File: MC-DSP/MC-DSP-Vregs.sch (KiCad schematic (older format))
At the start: 12 parts, among them IC1 R-78E5.0-0.5, T1 R-78E3.3-0.5

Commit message: updated top level of schematic with "to test" and "to do" notes
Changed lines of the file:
@@
 $Descr A4 11693 8268
 encoding utf-8
-Sheet 5 6
+Sheet 5 9
 Title ""
 Date ""
@@
 	6300 4225 6600 4225
 Connection ~ 6300 4225
-Text Notes 6850 3525 0    50   ~ 0
+Text Notes 2300 4000 0    50   ~ 0
 Toss this if dac buffs dont need it\n
 Text Notes 7175 5250 0    50   ~ 0

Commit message: ADC refs, FTDI changes, and more
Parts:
- removed C? (x2): 10 uF, Capacitor_SMD:C_0603_1608Metric, symbol Device:C_Small
- removed C? (x2): 4.7 uF, Capacitor_SMD:C_0603_1608Metric, symbol Device:C_Small
- removed C? (x2): 22 uF, Capacitor_SMD:C_0603_1608Metric, symbol Device:C_Small
- removed IC1: R-78E5.0-0.5, R78E5005, symbol R-78E5.0-0.5:R-78E5.0-0.5
- removed L? (x2): 12 uH, symbol Device:L_Small
- removed T1: R-78E3.3-0.5, R78E1205, symbol R-78E3.3-0.5:R-78E3.3-0.5
- added C? (x6): 2.2uF, symbol Device:C
- added C?: 10 uF, Capacitor_SMD:C_0603_1608Metric, symbol Device:C_Small
- added C?: 4.7 uF, Capacitor_SMD:C_0603_1608Metric, symbol Device:C_Small
- added C?: 22 uF, Capacitor_SMD:C_0603_1608Metric, symbol Device:C_Small
- added FB? (x3): Ferrite_Bead, symbol Device:Ferrite_Bead
- added L?: 12 uH, symbol Device:L_Small
- added T?: R-78E3.3-0.5, R78E1205, symbol R-78E3.3-0.5:R-78E3.3-0.5
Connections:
- net labels added: VDDA
- net labels removed: +5V
- wire segments 32 -> 40
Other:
- note added: "VDDA_3V3"
- note added: "VDD_1V2"
- note added: "VDD_3V3\n"
- note removed: "Toss this if dac buffs dont need it\n"
- moved on the sheet: C?

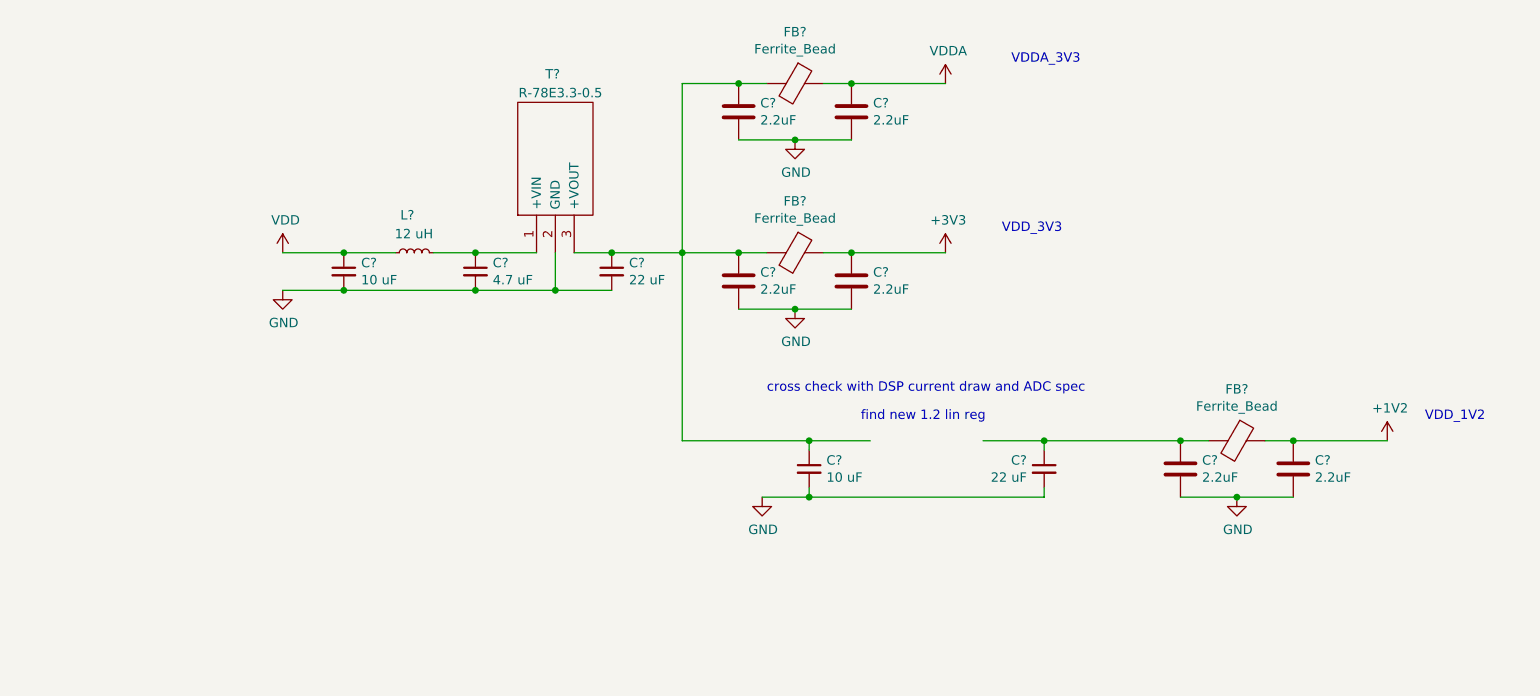
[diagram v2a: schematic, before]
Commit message: All parts labeled, just need to pick passives basically.
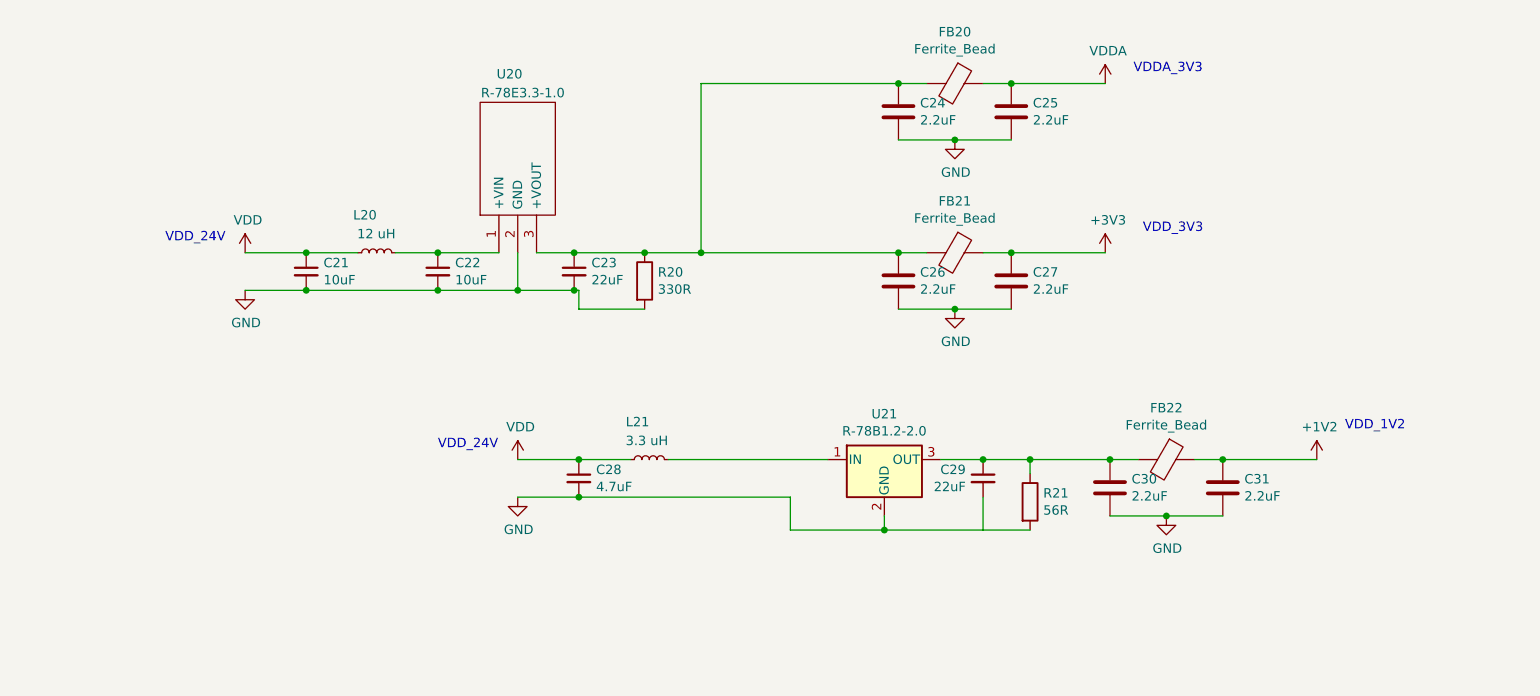
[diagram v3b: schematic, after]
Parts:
- removed C?: 10 uF, Capacitor_SMD:C_0603_1608Metric, symbol Device:C_Small
- added C28: 4.7uF, Capacitor_SMD:C_0201_0603Metric_Pad0.64x0.40mm_HandSolder, symbol Device:C_Small
- added L21: 3.3 uH, ?, symbol Device:L_Small
- added R20: 330R, Resistor_SMD:R_0603_1608Metric_Pad0.98x0.95mm_HandSolder, symbol Device:R
- added R21: 56R, Resistor_SMD:R_0603_1608Metric_Pad0.98x0.95mm_HandSolder, symbol Device:R
- added U21: R-78B1.2-2.0, Converter_DCDC:Converter_DCDC_RECOM_R-78B-2.0_THT, symbol Regulator_Switching:R-78B1.2-2.0
- C21: renamed from C?; value 10 uF -> 10uF; footprint Capacitor_SMD:C_0603_1608Metric -> Capacitor_SMD:C_0201_0603Metric_Pad0.64x0.40mm_HandSolder
- C22: renamed from C?; value 4.7 uF -> 10uF; footprint Capacitor_SMD:C_0603_1608Metric -> Capacitor_SMD:C_0201_0603Metric_Pad0.64x0.40mm_HandSolder
- C23, C29: renamed from C?; value 22 uF -> 22uF; footprint Capacitor_SMD:C_0603_1608Metric -> Capacitor_SMD:C_0201_0603Metric_Pad0.64x0.40mm_HandSolder
- C24, C25, C26, C27, C30, C31: renamed from C?; footprint (none) -> Capacitor_SMD:C_0201_0603Metric_Pad0.64x0.40mm_HandSolder
- FB20, FB21, FB22: renamed from FB?; footprint (none) -> ?
- L20: renamed from L?; footprint (none) -> ?
- U20: renamed from T?; value R-78E3.3-0.5 -> R-78E3.3-1.0
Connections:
- wire segments 40 -> 47
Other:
- note added: "VDD_24V"
- note removed: "cross check with DSP current draw and ADC spec"
- note removed: "find new 1.2 lin reg\n"
- moved on the sheet: C21, C22, C23, C24, C25, C26, C27, C29, C30, C31, FB20, FB21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

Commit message: DSP - added footprints and links to most parts
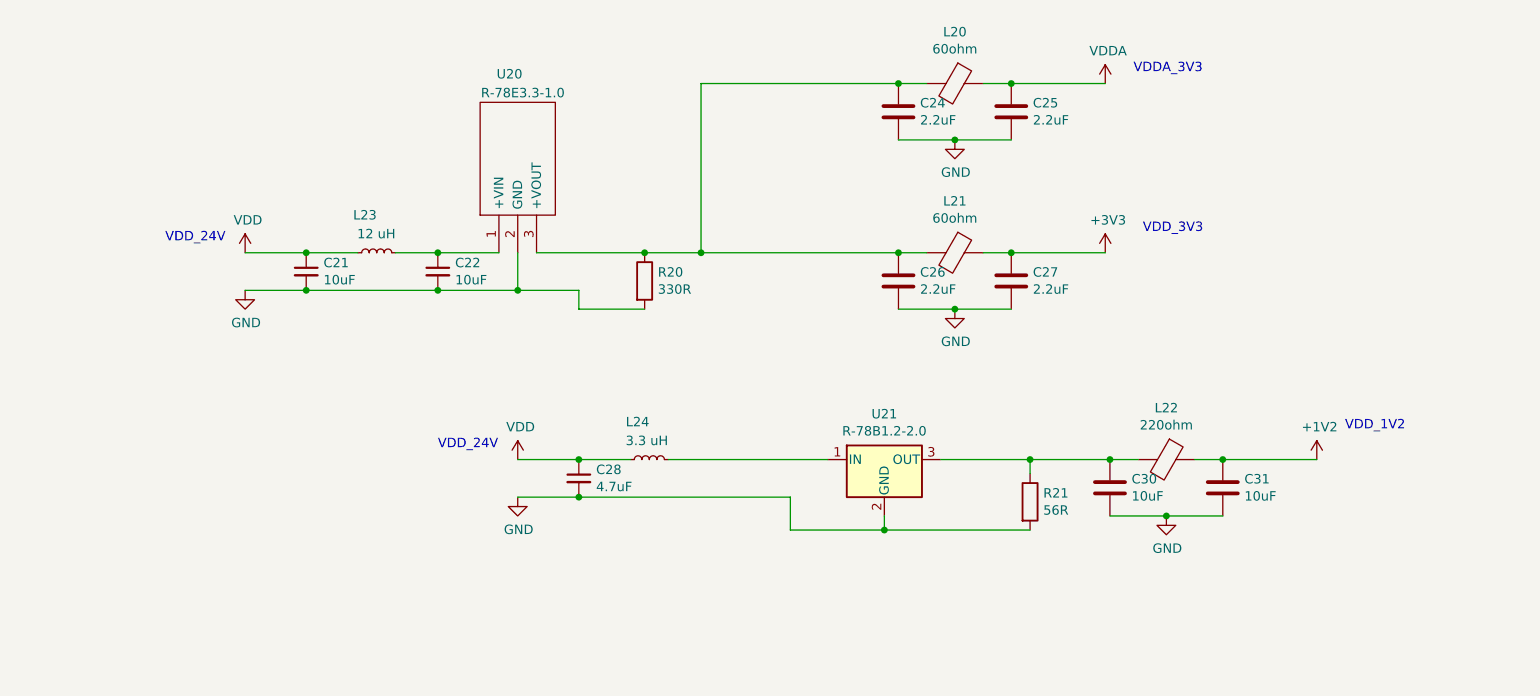
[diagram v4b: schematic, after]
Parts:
- removed C23, C29: 22uF, Capacitor_SMD:C_0201_0603Metric_Pad0.64x0.40mm_HandSolder, symbol Device:C_Small
- removed FB21: Ferrite_Bead, ?, symbol Device:Ferrite_Bead
- added L21: 60ohm, Inductor_SMD:L_0805_2012Metric_Pad1.05x1.20mm_HandSolder, symbol Device:Ferrite_Bead
- C30, C31: value 2.2uF -> 10uF
- L20: renamed from FB20; value Ferrite_Bead -> 60ohm; footprint ? -> Inductor_SMD:L_0805_2012Metric_Pad1.05x1.20mm_HandSolder
- L22: renamed from FB22; value Ferrite_Bead -> 220ohm; footprint ? -> Inductor_SMD:L_0805_2012Metric_Pad1.05x1.20mm_HandSolder
- L23: renamed from L20; footprint ? -> Inductor_THT:L_Radial_D8.7mm_P5.00mm_Fastron_07HCP
- L24: renamed from L21; footprint ? -> Inductor_THT:L_Radial_D8.7mm_P5.00mm_Fastron_07HCP
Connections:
- net +3V3: now also L21.1
- net at C24.2, C26.2, L20.2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: now also L21.2

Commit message: Removed clock buffer, misc leds, ethernet
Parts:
- C21, C22, C24, C25, C26, C27, C28, C30, C31: footprint Capacitor_SMD:C_0201_0603Metric_Pad0.64x0.40mm_HandSolder -> Capacitor_SMD:C_0603_1608Metric_Pad1.08x0.95mm_HandSolder
- U20: footprint R78E1205 -> Converter_DCDC:Converter_DCDC_RECOM_R-78B-2.0_THT
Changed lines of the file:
@@
 $Descr A4 11693 8268
 encoding utf-8
-Sheet 3 9
+Sheet 3 7
 Title ""
 Date ""
@@
 F 0 "C24" H 6885 2504 50  0000 R CNN
 F 1 "2.2uF" H 6885 2595 50  0000 R CNN
-F 2 "Capacitor_SMD:C_0201_0603Metric_Pad0.64x0.40mm_HandSolder" H 7038 2400 50  0001 C CNN
+F 2 "Capacitor_SMD:C_0603_1608Metric_Pad1.08x0.95mm_HandSolder" H 7038 2400 50  0001 C CNN
 F 3 "https://www.digikey.com/en/products/detail/samsung-electro-mechanics/CL10B225KP8NNNC/3886792" H 7000 2550 50  0001 C CNN
 	1    7000 2550
@@
 F 0 "C25" H 7715 2596 50  0000 L CNN
 F 1 "2.2uF" H 7715 2505 50  0000 L CNN
-F 2 "Capacitor_SMD:C_0201_0603Metric_Pad0.64x0.40mm_HandSolder" H 7638 2400 50  0001 C CNN
+F 2 "Capacitor_SMD:C_0603_1608Metric_Pad1.08x0.95mm_HandSolder" H 7638 2400 50  0001 C CNN
 F 3 "https://www.digikey.com/en/products/detail/samsung-electro-mechanics/CL10B225KP8NNNC/3886792" H 7600 2550 50  0001 C CNN
 	1    7600 2550
@@
 F 0 "C26" H 6885 3404 50  0000 R CNN
 F 1 "2.2uF" H 6885 3495 50  0000 R CNN
-F 2 "Capacitor_SMD:C_0201_0603Metric_Pad0.64x0.40mm_HandSolder" H 7038 3300 50  0001 C CNN
+F 2 "Capacitor_SMD:C_0603_1608Metric_Pad1.08x0.95mm_HandSolder" H 7038 3300 50  0001 C CNN
 F 3 "https://www.digikey.com/en/products/detail/samsung-electro-mechanics/CL10B225KP8NNNC/3886792" H 7000 3450 50  0001 C CNN
 	1    7000 3450
@@
 F 0 "C27" H 7715 3496 50  0000 L CNN
 F 1 "2.2uF" H 7715 3405 50  0000 L CNN
-F 2 "Capacitor_SMD:C_0201_0603Metric_Pad0.64x0.40mm_HandSolder" H 7638 3300 50  0001 C CNN
+F 2 "Capacitor_SMD:C_0603_1608Metric_Pad1.08x0.95mm_HandSolder" H 7638 3300 50  0001 C CNN
 F 3 "https://www.digikey.com/en/products/detail/samsung-electro-mechanics/CL10B225KP8NNNC/3886792" H 7600 3450 50  0001 C CNN
 	1    7600 3450
@@
 F 0 "C31" H 8840 4596 50  0000 L CNN
 F 1 "10uF" H 8840 4505 50  0000 L CNN
-F 2 "Capacitor_SMD:C_0201_0603Metric_Pad0.64x0.40mm_HandSolder" H 8763 4400 50  0001 C CNN
+F 2 "Capacitor_SMD:C_0603_1608Metric_Pad1.08x0.95mm_HandSolder" H 8763 4400 50  0001 C CNN
 F 3 "https://www.digikey.com/en/products/detail/kemet/C0603C104K5RECAUTO/6575893?s=N4IgjCBcpgLFoDGUBmBDANgZwKYBoQB7KAbRACYBmADgHYaQBdAgBwBcoQBlNgJwEsAdgHMQAXwJgAbAhDJI6bPiKkQlAJzlYM5iHaceAkeIIBacrPl8ArsuKQyAVhAF1TCSFNvocqDbuqEIxiHhYO4AAM1gBiTAQyPvwAJpymYBEWrByQIC4gbACeLDicSVjIIUA" H 8725 4550 50  0001 C CNN
 	1    8725 4550
@@
 F 0 "C30" H 8010 4504 50  0000 R CNN
 F 1 "10uF" H 8010 4595 50  0000 R CNN
-F 2 "Capacitor_SMD:C_0201_0603Metric_Pad0.64x0.40mm_HandSolder" H 8163 4400 50  0001 C CNN
+F 2 "Capacitor_SMD:C_0603_1608Metric_Pad1.08x0.95mm_HandSolder" H 8163 4400 50  0001 C CNN
 F 3 "https://www.digikey.com/en/products/detail/kemet/C0603C104K5RECAUTO/6575893?s=N4IgjCBcpgLFoDGUBmBDANgZwKYBoQB7KAbRACYBmADgHYaQBdAgBwBcoQBlNgJwEsAdgHMQAXwJgAbAhDJI6bPiKkQlAJzlYM5iHaceAkeIIBacrPl8ArsuKQyAVhAF1TCSFNvocqDbuqEIxiHhYO4AAM1gBiTAQyPvwAJpymYBEWrByQIC4gbACeLDicSVjIIUA" H 8125 4550 50  0001 C CNN
 	1    8125 4550
@@
 F 0 "C28" H 5392 4546 50  0000 L CNN
 F 1 "4.7uF" H 5392 4455 50  0000 L CNN
-F 2 "Capacitor_SMD:C_0201_0603Metric_Pad0.64x0.40mm_HandSolder" H 5300 4500 50  0001 C CNN
+F 2 "Capacitor_SMD:C_0603_1608Metric_Pad1.08x0.95mm_HandSolder" H 5300 4500 50  0001 C CNN
 F 3 "https://www.digikey.com/en/products/detail/tdk-corporation/C1608X5R1V475K080AC/3648577" H 5300 4500 50  0001 C CNN
 	1    5300 4500
@@
 F 0 "U20" V 5825 3175 50  0000 L CNN
 F 1 "R-78E3.3-1.0" V 5725 2950 50  0000 L CNN
-F 2 "R78E1205" H 5725 3400 50  0001 L CNN
+F 2 "Converter_DCDC:Converter_DCDC_RECOM_R-78B-2.0_THT" H 5725 3400 50  0001 L CNN
 F 3 "https://www.digikey.com/en/products/detail/recom-power/R-78E3-3-1-0/5327711" H 5725 3300 50  0001 L CNN
 	1    4875 3300
@@
 F 0 "C21" H 3942 3446 50  0000 L CNN
 F 1 "10uF" H 3942 3355 50  0000 L CNN
-F 2 "Capacitor_SMD:C_0201_0603Metric_Pad0.64x0.40mm_HandSolder" H 3850 3400 50  0001 C CNN
+F 2 "Capacitor_SMD:C_0603_1608Metric_Pad1.08x0.95mm_HandSolder" H 3850 3400 50  0001 C CNN
 F 3 "https://www.digikey.com/en/products/detail/kemet/C0603C104K5RECAUTO/6575893?s=N4IgjCBcpgLFoDGUBmBDANgZwKYBoQB7KAbRACYBmADgHYaQBdAgBwBcoQBlNgJwEsAdgHMQAXwJgAbAhDJI6bPiKkQlAJzlYM5iHaceAkeIIBacrPl8ArsuKQyAVhAF1TCSFNvocqDbuqEIxiHhYO4AAM1gBiTAQyPvwAJpymYBEWrByQIC4gbACeLDicSVjIIUA" H 3850 3400 50  0001 C CNN
 	1    3850 3400
@@
 F 0 "C22" H 4642 3446 50  0000 L CNN
 F 1 "10uF" H 4642 3355 50  0000 L CNN
-F 2 "Capacitor_SMD:C_0201_0603Metric_Pad0.64x0.40mm_HandSolder" H 4550 3400 50  0001 C CNN
+F 2 "Capacitor_SMD:C_0603_1608Metric_Pad1.08x0.95mm_HandSolder" H 4550 3400 50  0001 C CNN
 F 3 "https://www.digikey.com/en/products/detail/kemet/C0603C104K5RECAUTO/6575893?s=N4IgjCBcpgLFoDGUBmBDANgZwKYBoQB7KAbRACYBmADgHYaQBdAgBwBcoQBlNgJwEsAdgHMQAXwJgAbAhDJI6bPiKkQlAJzlYM5iHaceAkeIIBacrPl8ArsuKQyAVhAF1TCSFNvocqDbuqEIxiHhYO4AAM1gBiTAQyPvwAJpymYBEWrByQIC4gbACeLDicSVjIIUA" H 4550 3400 50  0001 C CNN
 	1    4550 3400

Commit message: added backplane connector, changed right angle headers, added FP for bigger reg caps, all ICs arranged, routed isolated section.
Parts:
- C21, C22, C28: footprint Capacitor_SMD:C_0603_1608Metric_Pad1.08x0.95mm_HandSolder -> Capacitor_SMD:C_1210_3225Metric
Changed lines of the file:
@@
 $Descr A4 11693 8268
 encoding utf-8
-Sheet 3 7
+Sheet 2 6
 Title ""
 Date ""
@@
 F 0 "C28" H 5392 4546 50  0000 L CNN
 F 1 "4.7uF" H 5392 4455 50  0000 L CNN
-F 2 "Capacitor_SMD:C_0603_1608Metric_Pad1.08x0.95mm_HandSolder" H 5300 4500 50  0001 C CNN
+F 2 "Capacitor_SMD:C_1210_3225Metric" H 5300 4500 50  0001 C CNN
 F 3 "https://www.digikey.com/en/products/detail/tdk-corporation/C1608X5R1V475K080AC/3648577" H 5300 4500 50  0001 C CNN
 	1    5300 4500
@@
 F 0 "C21" H 3942 3446 50  0000 L CNN
 F 1 "10uF" H 3942 3355 50  0000 L CNN
-F 2 "Capacitor_SMD:C_0603_1608Metric_Pad1.08x0.95mm_HandSolder" H 3850 3400 50  0001 C CNN
+F 2 "Capacitor_SMD:C_1210_3225Metric" H 3850 3400 50  0001 C CNN
 F 3 "https://www.digikey.com/en/products/detail/kemet/C0603C104K5RECAUTO/6575893?s=N4IgjCBcpgLFoDGUBmBDANgZwKYBoQB7KAbRACYBmADgHYaQBdAgBwBcoQBlNgJwEsAdgHMQAXwJgAbAhDJI6bPiKkQlAJzlYM5iHaceAkeIIBacrPl8ArsuKQyAVhAF1TCSFNvocqDbuqEIxiHhYO4AAM1gBiTAQyPvwAJpymYBEWrByQIC4gbACeLDicSVjIIUA" H 3850 3400 50  0001 C CNN
 	1    3850 3400
@@
 F 0 "C22" H 4642 3446 50  0000 L CNN
 F 1 "10uF" H 4642 3355 50  0000 L CNN
-F 2 "Capacitor_SMD:C_0603_1608Metric_Pad1.08x0.95mm_HandSolder" H 4550 3400 50  0001 C CNN
+F 2 "Capacitor_SMD:C_1210_3225Metric" H 4550 3400 50  0001 C CNN
 F 3 "https://www.digikey.com/en/products/detail/kemet/C0603C104K5RECAUTO/6575893?s=N4IgjCBcpgLFoDGUBmBDANgZwKYBoQB7KAbRACYBmADgHYaQBdAgBwBcoQBlNgJwEsAdgHMQAXwJgAbAhDJI6bPiKkQlAJzlYM5iHaceAkeIIBacrPl8ArsuKQyAVhAF1TCSFNvocqDbuqEIxiHhYO4AAM1gBiTAQyPvwAJpymYBEWrByQIC4gbACeLDicSVjIIUA" H 4550 3400 50  0001 C CNN
 	1    4550 3400

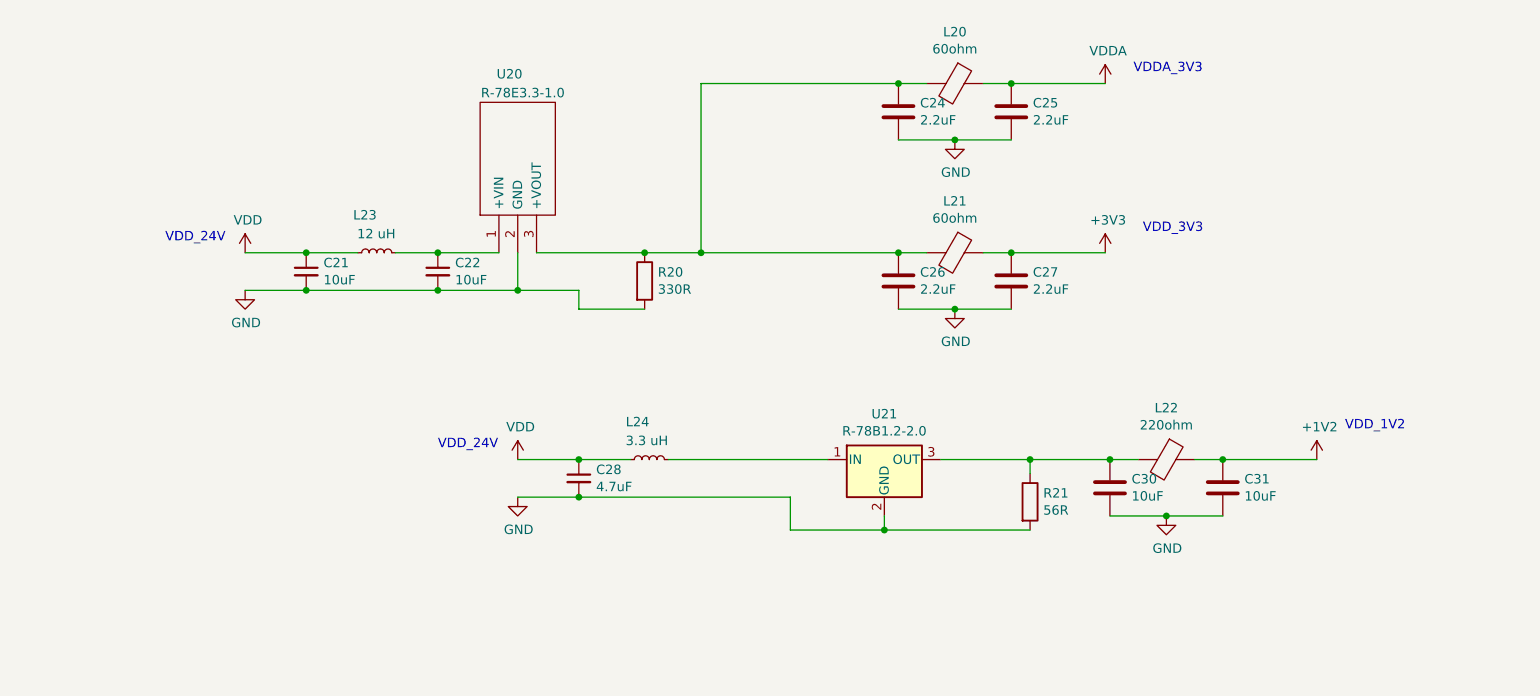
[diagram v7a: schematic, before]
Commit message: Total overhaul of power planes. Routed whole Analog section, middle of digital section.
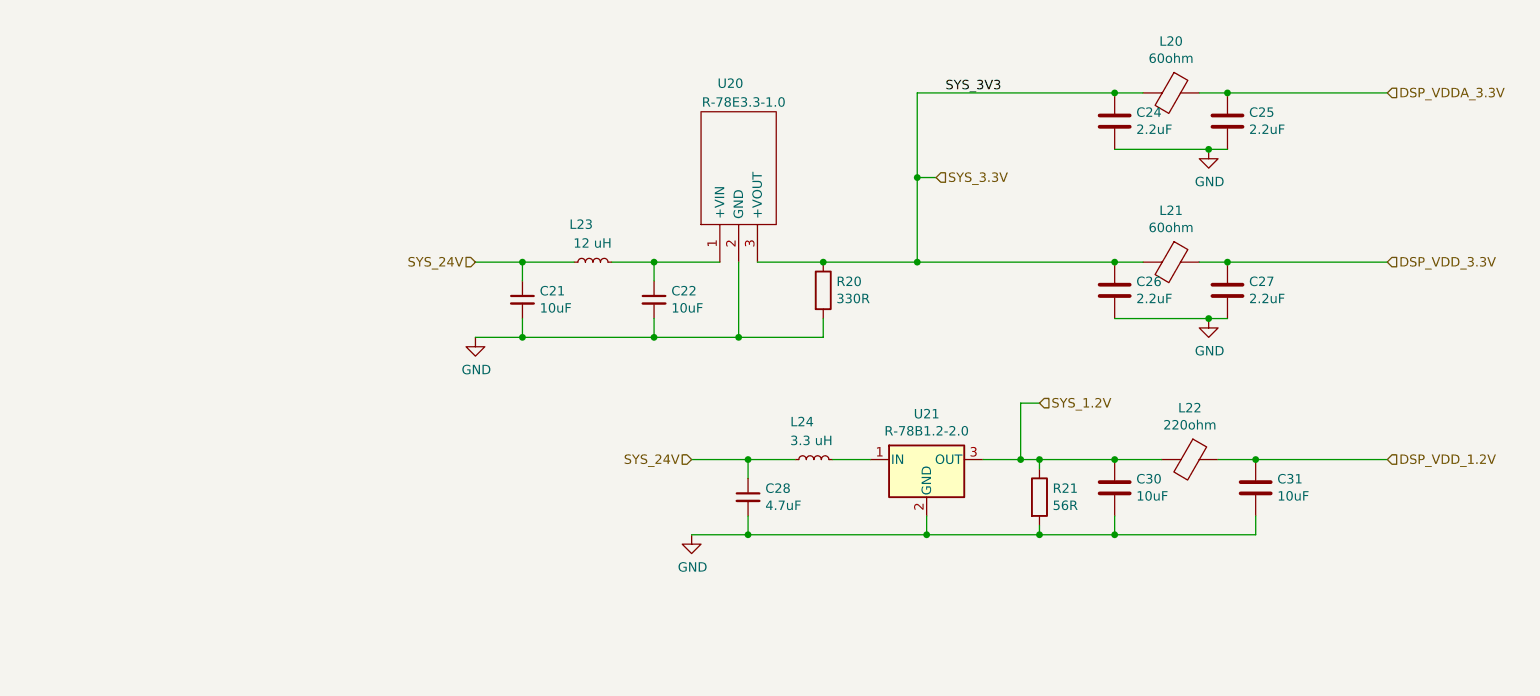
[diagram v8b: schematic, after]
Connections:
- net SYS_3.3V: now reaches C24.2, C26.2, L20.2, L21.2, R20.1, U20.3 (+VOUT)
- net SYS_1.2V: now reaches C30.2, L22.2, R21.1, U21.3 (OUT)
- net +1V2 renamed DSP_VDD_1.2V
- net +3V3 renamed DSP_VDD_3.3V
- net VDD renamed SYS_24V
- net VDDA renamed DSP_VDDA_3.3V
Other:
- note removed: "VDDA_3V3"
- note removed: "VDD_1V2"
- note removed: "VDD_24V"
- note removed: "VDD_3V3\n"
- moved on the sheet: C21, C22, C24, C25, C26, C27, C28, C30, C31, L20, L21, L22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
